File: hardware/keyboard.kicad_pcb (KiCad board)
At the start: 2 copper layers, 321.6 x 135 mm, 172 parts, among them J1 USB_OTG, U1 ATMEGA32U4-AU, U2 MCP23018_SSOP, Y1 16MHz

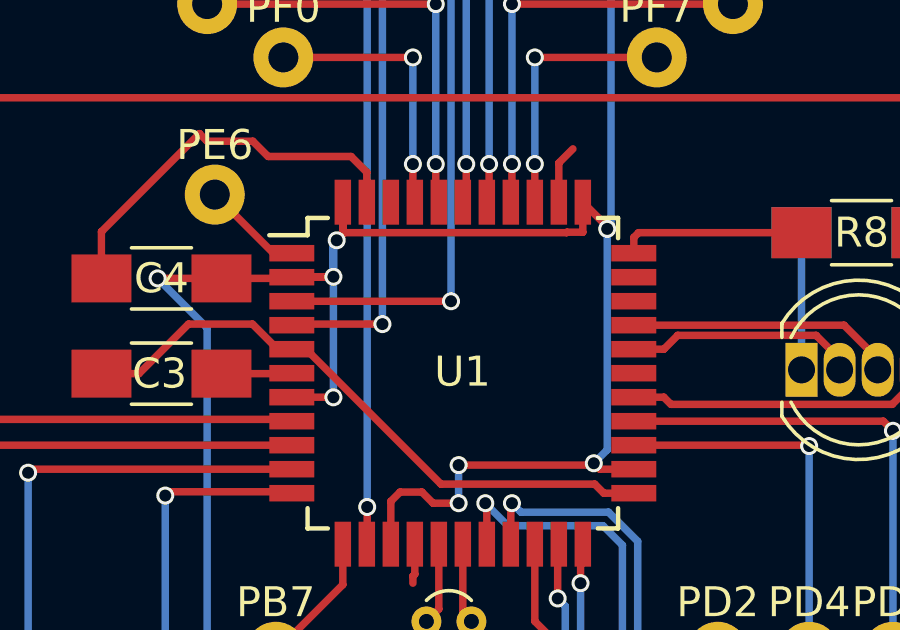
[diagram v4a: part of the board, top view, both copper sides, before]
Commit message: Update mounting hole references to ''
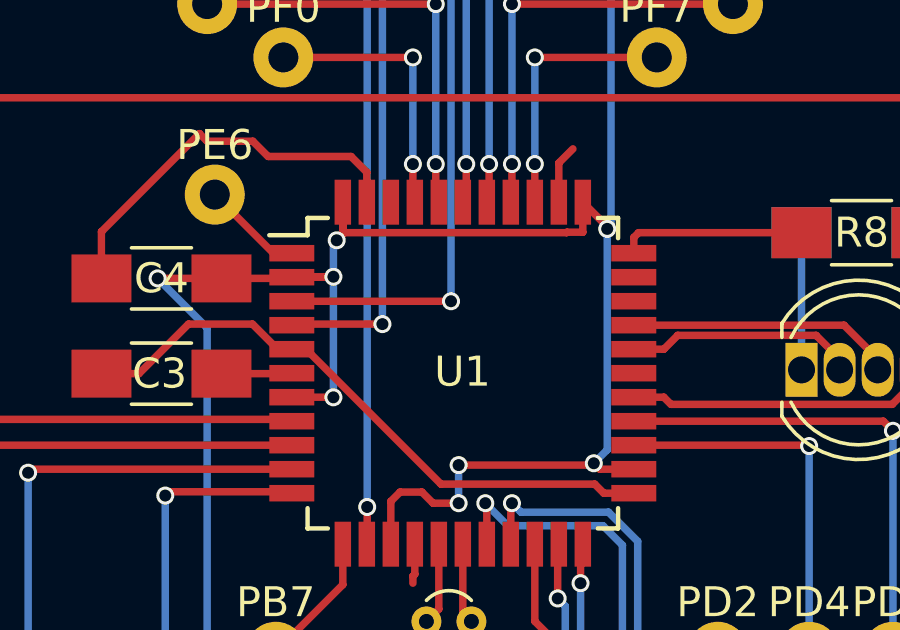
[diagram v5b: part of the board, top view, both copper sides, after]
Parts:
- removed REF** (x9): MountingHole_3.2mm_M3, MountingHole_3.2mm_M3
- added ?: MountingHole_3.2mm_M3, MountingHole_3.2mm_M3, F.Cu at (230.9, 148.9)
- added ?: MountingHole_3.2mm_M3, MountingHole_3.2mm_M3, F.Cu at (127.1, 148.9)
- added ?: MountingHole_3.2mm_M3, MountingHole_3.2mm_M3, F.Cu at (179.0, 155.9)
- added ?: MountingHole_3.2mm_M3, MountingHole_3.2mm_M3, F.Cu at (335.5, 130.5)
- added ?: MountingHole_3.2mm_M3, MountingHole_3.2mm_M3, F.Cu at (22.5, 130.5)
- added ?: MountingHole_3.2mm_M3, MountingHole_3.2mm_M3, F.Cu at (316.7, 28.9)
- added ?: MountingHole_3.2mm_M3, MountingHole_3.2mm_M3, F.Cu at (230.7, 28.9)
- added ?: MountingHole_3.2mm_M3, MountingHole_3.2mm_M3, F.Cu at (127.3, 28.9)
- added ?: MountingHole_3.2mm_M3, MountingHole_3.2mm_M3, F.Cu at (41.3, 28.9)
- renumbered D1 to ?
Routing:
- net +5V: track 141.4 -> 139.3 mm
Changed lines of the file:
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@@
     (links 256)
     (no_connects 0)
-    (area 13.09439 23.434285 344.905608 190.075001)
+    (area 0.254 20.32 347.218001 190.075001)
     (thickness 1.6)
-    (drawings 8)
-    (tracks 804)
+    (drawings 6)
+    (tracks 802)
     (zones 0)
     (modules 172)
@@
     (descr "Mounting Hole 3.2mm, no annular, M3")
     (tags "mounting hole 3.2mm no annular m3")
-    (fp_text reference REF** (at 0 -4.2) (layer F.SilkS) hide
+    (fp_text reference "" (at 0 -4.2) (layer F.SilkS)
       (effects (font (size 1 1) (thickness 0.15)))
     )
@@
     (descr "Mounting Hole 3.2mm, no annular, M3")
     (tags "mounting hole 3.2mm no annular m3")
-    (fp_text reference REF** (at 0 -4.2) (layer F.SilkS) hide
+    (fp_text reference "" (at 0 -4.2) (layer F.SilkS)
       (effects (font (size 1 1) (thickness 0.15)))
     )
@@
     (descr "Mounting Hole 3.2mm, no annular, M3")
     (tags "mounting hole 3.2mm no annular m3")
-    (fp_text reference REF** (at 0 -4.2) (layer F.SilkS) hide
+    (fp_text reference "" (at 0 -4.2) (layer F.SilkS)
       (effects (font (size 1 1) (thickness 0.15)))
     )
@@
     (descr "Mounting Hole 3.2mm, no annular, M3")
     (tags "mounting hole 3.2mm no annular m3")
-    (fp_text reference REF** (at 0 -4.2) (layer F.SilkS) hide
+    (fp_text reference "" (at 0 -4.2) (layer F.SilkS)
       (effects (font (size 1 1) (thickness 0.15)))
     )
@@
     (descr "Mounting Hole 3.2mm, no annular, M3")
     (tags "mounting hole 3.2mm no annular m3")
-    (fp_text reference REF** (at 0 -4.2) (layer F.SilkS) hide
+    (fp_text reference "" (at 0 -4.2) (layer F.SilkS)
       (effects (font (size 1 1) (thickness 0.15)))
     )
@@
     (descr "Mounting Hole 3.2mm, no annular, M3")
     (tags "mounting hole 3.2mm no annular m3")
-    (fp_text reference REF** (at 0 -4.2) (layer F.SilkS) hide
+    (fp_text reference "" (at 0 -4.2) (layer F.SilkS)
       (effects (font (size 1 1) (thickness 0.15)))
     )
@@
     (descr "Mounting Hole 3.2mm, no annular, M3")
     (tags "mounting hole 3.2mm no annular m3")
-    (fp_text reference REF** (at 0 -4.2) (layer F.SilkS) hide
+    (fp_text reference "" (at 0 -4.2) (layer F.SilkS)
       (effects (font (size 1 1) (thickness 0.15)))
     )
@@
     (descr "Mounting Hole 3.2mm, no annular, M3")
     (tags "mounting hole 3.2mm no annular m3")
-    (fp_text reference REF** (at 0 -4.2) (layer F.SilkS) hide
+    (fp_text reference "" (at 0 -4.2) (layer F.SilkS)
       (effects (font (size 1 1) (thickness 0.15)))
     )
@@
     (descr "Mounting Hole 3.2mm, no annular, M3")
     (tags "mounting hole 3.2mm no annular m3")
-    (fp_text reference REF** (at 0 -4.2) (layer F.SilkS) hide
+    (fp_text reference "" (at 0 -4.2) (layer F.SilkS)
       (effects (font (size 1 1) (thickness 0.15)))
     )
@@
     (tags SOD-123)
     (attr smd)
-    (fp_text reference D1 (at 0 2 170) (layer B.SilkS)
+    (fp_text reference "" (at 0 2 170) (layer B.SilkS)
       (effects (font (size 1 1) (thickness 0.15)) (justify mirror))
     )
@@
   (gr_line (start 18.191942 133.462701) (end 168.276643 159.926683) (layer Edge.Cuts) (width 0.15))
   (gr_line (start 37.336653 24.887647) (end 18.191942 133.462701) (layer Edge.Cuts) (width 0.15))
-  (gr_line (start 179 40) (end 179 190) (layer Dwgs.User) (width 0.15))
-  (gr_line (start 179 40) (end 179 190) (layer Dwgs.User) (width 0.15))
   (segment (start 182.664 73.368) (end 183.134 72.898) (width 0.25) (layer F.Cu) (net 1))
-  (segment (start 182.664 74.676) (end 182.664 73.368) (width 0.25) (layer F.Cu) (net 1))
+  (segment (start 182.664 74.676) (end 182.664 73.368) (width 0.25) (layer F.Cu) (net 1) (status 10))
   (segment (start 194.754 73.342) (end 194.564 73.152) (width 0.25) (layer F.Cu) (net 1))
-  (segment (start 194.754 75.692) (end 194.754 73.342) (width 0.25) (layer F.Cu) (net 1))
+  (segment (start 194.754 75.692) (end 194.754 73.342) (width 0.25) (layer F.Cu) (net 1) (status 10))
   (segment (start 178.737 84.074) (end 183.862 84.074) (width 0.25) (layer F.Cu) (net 1))
   (segment (start 183.862 84.074) (end 184.164 84.376) (width 0.25) (layer F.Cu) (net 1))
-  (segment (start 184.164 84.376) (end 185.164 84.376) (width 0.25) (layer F.Cu) (net 1))
-  (segment (start 173.764 79.576) (end 174.239 79.576) (width 0.25) (layer F.Cu) (net 1))
-  (segment (start 174.239 79.576) (end 178.737 84.074) (width 0.25) (layer F.Cu) (net 1))
+  (segment (start 184.164 84.376) (end 185.164 84.376) (width 0.25) (layer F.Cu) (net 1) (status 20))
+  (segment (start 173.764 79.576) (end 174.239 79.576) (width 0.25) (layer F.Cu) (net 1) (status 30))
+  (segment (start 174.239 79.576) (end 178.737 84.074) (width 0.25) (layer F.Cu) (net 1) (status 10))
   (segment (start 177.8 87.14) (end 177.8 87.376) (width 0.25) (layer F.Cu) (net 1))
-  (segment (start 177.864 86.076) (end 177.864 87.076) (width 0.25) (layer F.Cu) (net 1))
+  (segment (start 177.864 86.076) (end 177.864 87.076) (width 0.25) (layer F.Cu) (net 1) (status 10))
   (segment (start 177.864 87.076) (end 177.8 87.14) (width 0.25) (layer F.Cu) (net 1))
   (segment (start 176.948 110.58) (end 181.07 106.458) (width 0.25) (layer F.Cu) (net 1))
-  (segment (start 181.07 106.458) (end 181.07 102.362) (width 0.25) (layer F.Cu) (net 1))
-  (segment (start 175.21 110.58) (end 176.948 110.58) (width 0.25) (layer F.Cu) (net 1))
+  (segment (start 181.07 106.458) (end 181.07 102.362) (width 0.25) (layer F.Cu) (net 1) (status 20))
+  (segment (start 175.21 110.58) (end 176.948 110.58) (width 0.25) (layer F.Cu) (net 1) (status 10))
   (segment (start 170.686 72.39) (end 167.418 75.658) (width 0.25) (layer F.Cu) (net 1))
-  (segment (start 167.418 75.658) (end 167.418 77.216) (width 0.25) (layer F.Cu) (net 1))
+  (segment (start 167.418 75.658) (end 167.418 77.216) (width 0.25) (layer F.Cu) (net 1) (status 20))
   (segment (start 172.466 72.644) (end 170.94 72.644) (width 0.25) (layer F.Cu) (net 1))
   (segment (start 170.94 72.644) (end 170.686 72.39) (width 0.25) (layer F.Cu) (net 1))
   (segment (start 172.974 73.152) (end 172.466 72.644) (width 0.25) (layer F.Cu) (net 1))
   (segment (start 175.74 73.152) (end 172.974 73.152) (width 0.25) (layer F.Cu) (net 1))
-  (segment (start 176.264 74.676) (end 176.264 73.676) (width 0.25) (layer F.Cu) (net 1))
+  (segment (start 176.264 74.676) (end 176.264 73.676) (width 0.25) (layer F.Cu) (net 1) (status 10))
   (segment (start 176.264 73.676) (end 175.74 73.152) (width 0.25) (layer F.Cu) (net 1))
   (segment (start 172.453 78.74) (end 170.319 78.74) (width 0.25) (layer F.Cu) (net 1))
   (segment (start 170.319 78.74) (end 168.668 80.391) (width 0.25) (layer F.Cu) (net 1))
-  (segment (start 168.668 80.391) (end 167.418 80.391) (width 0.25) (layer F.Cu) (net 1))
-  (segment (start 173.764 79.576) (end 173.289 79.576) (width 0.25) (layer F.Cu) (net 1))
-  (segment (start 173.289 79.576) (end 172.453 78.74) (width 0.25) (layer F.Cu) (net 1))
+  (segment (start 168.668 80.391) (end 167.418 80.391) (width 0.25) (layer F.Cu) (net 1) (status 20))
+  (segment (start 173.764 79.576) (end 173.289 79.576) (width 0.25) (layer F.Cu) (net 1) (status 30))
+  (segment (start 173.289 79.576) (end 172.453 78.74) (width 0.25) (layer F.Cu) (net 1) (status 10))
   (segment (start 181.5 91) (end 181.5 90.8) (width 0.25) (layer F.Cu) (net 2) (status 30))
   (segment (start 181.5 90.8) (end 179.75 89.05) (width 0.25) (layer F.Cu) (net 2) (status 30))
@@
   (segment (start 178.664 86.076) (end 178.664 88.236) (width 0.25) (layer F.Cu) (net 3) (status 10))
   (segment (start 178.664 88.236) (end 178.25 88.65) (width 0.25) (layer F.Cu) (net 3) (status 20))
-  (segment (start 175.464 74.676) (end 175.464 75.742) (width 0.25) (layer F.Cu) (net 4))
+  (segment (start 175.464 74.676) (end 175.464 75.742) (width 0.25) (layer F.Cu) (net 4) (status 10))
   (segment (start 175.464 75.742) (end 175.26 75.946) (width 0.25) (layer F.Cu) (net 4))
   (segment (start 175.15 77.16) (end 175.15 76.056) (width 0.25) (layer B.Cu) (net 4))
   (segment (start 175.15 76.056) (end 175.26 75.946) (width 0.25) (layer B.Cu) (net 4))
-  (segment (start 175.15 77.16) (end 175.15 76.09) (width 0.25) (layer B.Cu) (net 4))
-  (segment (start 175.15 81.18) (end 175.15 76.09) (width 0.25) (layer B.Cu) (net 4))
-  (segment (start 173.764 77.176) (end 175.134 77.176) (width 0.25) (layer F.Cu) (net 4))
+  (segment (start 175.15 77.16) (end 175.15 81.18) (width 0.25) (layer B.Cu) (net 4))
+  (segment (start 173.764 77.176) (end 175.134 77.176) (width 0.25) (layer F.Cu) (net 4) (status 10))
   (segment (start 175.134 77.176) (end 175.15 77.16) (width 0.25) (layer F.Cu) (net 4))
   (segment (start 184.404 38.862) (end 184.404 75.438) (width 0.25) (layer B.Cu) (net 4) (status 10))
@@
   (segment (start 181.61 38.862) (end 184.404 38.862) (width 0.25) (layer F.Cu) (net 4) (status 30))
   (via (at 175.15 77.16) (size 0.6) (drill 0.4) (layers F.Cu B.Cu) (net 4))
-  (segment (start 175.514 75.692) (end 182.923 75.692) (width 0.25) (layer F.Cu) (net 4))
+  (segment (start 175.48 75.692) (end 182.923 75.692) (width 0.25) (layer F.Cu) (net 4))
   (segment (start 175.464 74.676) (end 175.464 75.676) (width 0.25) (layer F.Cu) (net 4) (status 10))
   (segment (start 175.464 75.676) (end 175.48 75.692) (width 0.25) (layer F.Cu) (net 4))
-  (segment (start 175.48 75.692) (end 175.514 75.692) (width 0.25) (layer F.Cu) (net 4))
   (segment (start 182.923 75.692) (end 182.939 75.676) (width 0.25) (layer F.Cu) (net 4))
   (segment (start 182.939 75.676) (end 183.464 75.676) (width 0.25) (layer F.Cu) (net 4))

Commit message: finish V2
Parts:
- removed the ? at (41.8, 36.9)
- removed D65: LED_CRGB, LEDs:LED_D5.0mm-4
- removed GND, SCL, SDA, VCC: CONN_01X01, keyboard-modules:CONN_1
- added D1: D_Small, Diodes_SMD:D_SOD-123, B.Cu at (41.8, 36.9)
- added D99: LED_ARGB, LEDs:LED_D5.0mm-4-v2, F.Cu at (166.9, 35.8)
- added R1: 1k, Resistors_SMD:R_1206_HandSoldering, F.Cu at (166.6, 42.4)
- added R3: 1k, Resistors_SMD:R_1206_HandSoldering, F.Cu at (171.2, 42.4)
- R2: moved to F.Cu
- moved R2 41.0 mm to (168.9, 42.4), turned to 270 degrees
- moved R8 5.15 mm to (187.7, 74.7), turned to 270 degrees
- moved D61 0.25 mm to (149.6, 134.1)
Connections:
- R2 pad 2: GND -> LED2
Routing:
- net LED3: track 10.2 -> 70.4 mm, vias 0 -> 2
- net LED2: track 9.32 -> 65.7 mm, vias 0 -> 2
- net LED1: track 7.85 -> 63.7 mm, vias 0 -> 2
- net +5V: track 139.3 -> 155.9 mm, vias 11 -> 12
- net GND: track 51.6 -> 62.7 mm
- net Net-(D99-Pad2): track 0.00 -> 5.04 mm
- net Net-(D99-Pad4): track 0.00 -> 4.78 mm
- net Net-(R8-Pad2): track 6.29 -> 2.78 mm
- net SDA: track 43.7 -> 42.3 mm
- net SCL: track 42.5 -> 41.1 mm
- net Net-(D62-Pad2): track 3.30 -> 4.18 mm

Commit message: Update schematic, WIP fixes + adding test points
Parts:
- removed ? (x9): MountingHole_3.2mm_M3, MountingHole_3.2mm_M3
- removed PB7, PD2, PD3, PD4, PD5, PD6, PE6, PF0, PF1, PF4, PF5, PF6, PF7: CONN_01X01, keyboard-modules:CONN_1
- added J2: CONN_01X05, Pin_Headers:Pin_Header_Straight_1x05_Pitch1.27mm, F.Cu at (156.5, 81.5)
- added J3: CONN_01X04, Pin_Headers:Pin_Header_Straight_1x04_Pitch1.27mm, F.Cu at (187.7, 99.3)
- added J4: CONN_01X07, Pin_Headers:Pin_Header_Straight_1x07_Pitch1.27mm, F.Cu at (159.5, 60.2)
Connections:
- net Net-(R8-Pad2) renamed /PE2
- U1 pad 1: /PE6 -> (no net)
- U1 pad 12: Net-(PB7-Pad1) -> ROW4
- U1 pad 20: /PD2 -> (no net)
- U1 pad 21: /PD3 -> (no net)
- U1 pad 22: /PD5 -> (no net)
- U1 pad 25: /PD4 -> (no net)
- U1 pad 26: /PD6 -> (no net)
- U1 pad 27: LED3 -> (no net)
- U1 pad 28: (no net) -> LED1
- U1 pad 29: LED1 -> LED2
- U1 pad 30: LED2 -> LED3
- U1 pad 40: /PF1 -> (no net)
- U1 pad 41: /PF0 -> (no net)
- U2 pad 1: +5V -> GND
- U2 pad 10: GND -> +5V
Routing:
- net ROW4: track 0.00 -> 19.2 mm, vias 0 -> 1
- net /PD6: track 16.1 -> 0.00 mm, vias 1 -> 0
- net /PD5: track 14.5 -> 0.00 mm, vias 2 -> 0
- net /PF4: track 14.5 -> 0.16 mm, vias 2 -> 0
- net /PF1: track 14.3 -> 0.00 mm, vias 2 -> 0
- net /PF6: track 14.0 -> 0.05 mm, vias 2 -> 0
- net /PF5: track 14.0 -> 0.11 mm, vias 2 -> 0
- net ROW3: track 396.4 -> 409.8 mm
- net /PD4: track 12.7 -> 0.00 mm, vias 1 -> 0
- net /PD3: track 12.6 -> 0.00 mm, vias 2 -> 0
- net /PF0: track 9.17 -> 0.00 mm, vias 2 -> 0
- net /PD2: track 9.09 -> 0.00 mm
- net /PF7: track 8.89 -> 0.00 mm, vias 2 -> 0
- net ROW2: track 359.4 -> 368.0 mm
- net LED3: track 70.4 -> 78.0 mm
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- removed copper zone on B.Cu, net GND
- removed copper zone on F.Cu, net GND

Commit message: Add mounting holes back
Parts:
- added ?: MountingHole_3.2mm_M3, MountingHole_3.2mm_M3, F.Cu at (230.9, 148.9)
- added ?: MountingHole_3.2mm_M3, MountingHole_3.2mm_M3, F.Cu at (127.1, 148.9)
- added ?: MountingHole_3.2mm_M3, MountingHole_3.2mm_M3, F.Cu at (179.0, 155.9)
- added ?: MountingHole_3.2mm_M3, MountingHole_3.2mm_M3, F.Cu at (335.5, 130.5)
- added ?: MountingHole_3.2mm_M3, MountingHole_3.2mm_M3, F.Cu at (22.5, 130.5)
- added ?: MountingHole_3.2mm_M3, MountingHole_3.2mm_M3, F.Cu at (316.7, 28.9)
- added ?: MountingHole_3.2mm_M3, MountingHole_3.2mm_M3, F.Cu at (230.7, 28.9)
- added ?: MountingHole_3.2mm_M3, MountingHole_3.2mm_M3, F.Cu at (127.3, 28.9)
- added ?: MountingHole_3.2mm_M3, MountingHole_3.2mm_M3, F.Cu at (41.3, 28.9)
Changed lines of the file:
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@@
   (general
     (links 256)
-    (no_connects 21)
-    (area 18.116941 24.812646 339.883057 160.001684)
+    (no_connects 20)
+    (area 13.09439 23.434285 344.905608 161.001683)
     (thickness 1.6)
     (drawings 6)
     (tracks 785)
     (zones 0)
-    (modules 151)
+    (modules 160)
     (nets 109)
   )
@@
     (add_net SDA)
   )
+  (module MountingHole_3.2mm_M3 (layer F.Cu)
+    (at 230.863401 148.938904)
+    (descr "Mounting Hole 3.2mm, no annular, M3")
+    (tags "mounting hole 3.2mm no annular m3")
+    (fp_text reference "" (at 0 -4.2) (layer F.SilkS)
+      (effects (font (size 1 1) (thickness 0.15)))
+    )
+    (fp_text value MountingHole_3.2mm_M3 (at 0 4.2) (layer F.Fab)
+      (effects (font (size 1 1) (thickness 0.15)))
+    )
+    (fp_circle (center 0 0) (end 3.45 0) (layer F.CrtYd) (width 0.05))
+    (fp_circle (center 0 0) (end 3.2 0) (layer Cmts.User) (width 0.15))
+    (pad 1 np_thru_hole circle (at 0 0) (size 3.2 3.2) (drill 3.2) (layers *.Cu *.Mask))
+  )
+  (module MountingHole_3.2mm_M3 (layer F.Cu)
+    (at 127.136596 148.938904)
+    (descr "Mounting Hole 3.2mm, no annular, M3")
+    (tags "mounting hole 3.2mm no annular m3")
+    (fp_text reference "" (at 0 -4.2) (layer F.SilkS)
+      (effects (font (size 1 1) (thickness 0.15)))
+    )
+    (fp_text value MountingHole_3.2mm_M3 (at 0 4.2) (layer F.Fab)
+      (effects (font (size 1 1) (thickness 0.15)))
+    )
+    (fp_circle (center 0 0) (end 3.45 0) (layer F.CrtYd) (width 0.05))
+    (fp_circle (center 0 0) (end 3.2 0) (layer Cmts.User) (width 0.15))
+    (pad 1 np_thru_hole circle (at 0 0) (size 3.2 3.2) (drill 3.2) (layers *.Cu *.Mask))
+  )
+  (module MountingHole_3.2mm_M3 (layer F.Cu)
+    (at 178.999998 155.926683)
+    (descr "Mounting Hole 3.2mm, no annular, M3")
+    (tags "mounting hole 3.2mm no annular m3")
+    (fp_text reference "" (at 0 -4.2) (layer F.SilkS)
+      (effects (font (size 1 1) (thickness 0.15)))
+    )
+    (fp_text value MountingHole_3.2mm_M3 (at 0 4.2) (layer F.Fab)
+      (effects (font (size 1 1) (thickness 0.15)))
+    )
+    (fp_circle (center 0 0) (end 3.45 0) (layer F.CrtYd) (width 0.05))
+    (fp_circle (center 0 0) (end 3.2 0) (layer Cmts.User) (width 0.15))
+    (pad 1 np_thru_hole circle (at 0 0) (size 3.2 3.2) (drill 3.2) (layers *.Cu *.Mask))
+  )
+  (module MountingHole_3.2mm_M3 (layer F.Cu)
+    (at 335.548465 130.480103)
+    (descr "Mounting Hole 3.2mm, no annular, M3")
+    (tags "mounting hole 3.2mm no annular m3")
+    (fp_text reference "" (at 0 -4.2) (layer F.SilkS)
+      (effects (font (size 1 1) (thickness 0.15)))
+    )
+    (fp_text value MountingHole_3.2mm_M3 (at 0 4.2) (layer F.Fab)
+      (effects (font (size 1 1) (thickness 0.15)))
+    )
+    (fp_circle (center 0 0) (end 3.45 0) (layer F.CrtYd) (width 0.05))
+    (fp_circle (center 0 0) (end 3.2 0) (layer Cmts.User) (width 0.15))
+    (pad 1 np_thru_hole circle (at 0 0) (size 3.2 3.2) (drill 3.2) (layers *.Cu *.Mask))
+  )
+  (module MountingHole_3.2mm_M3 (layer F.Cu)
+    (at 22.451533 130.480103)
+    (descr "Mounting Hole 3.2mm, no annular, M3")
+    (tags "mounting hole 3.2mm no annular m3")
+    (fp_text reference "" (at 0 -4.2) (layer F.SilkS)
+      (effects (font (size 1 1) (thickness 0.15)))
+    )
+    (fp_text value MountingHole_3.2mm_M3 (at 0 4.2) (layer F.Fab)
+      (effects (font (size 1 1) (thickness 0.15)))
+    )
+    (fp_circle (center 0 0) (end 3.45 0) (layer F.CrtYd) (width 0.05))
+    (fp_circle (center 0 0) (end 3.2 0) (layer Cmts.User) (width 0.15))
+    (pad 1 np_thru_hole circle (at 0 0) (size 3.2 3.2) (drill 3.2) (layers *.Cu *.Mask))
+  )
+  (module MountingHole_3.2mm_M3 (layer F.Cu)
+    (at 316.663345 28.887647)
+    (descr "Mounting Hole 3.2mm, no annular, M3")
+    (tags "mounting hole 3.2mm no annular m3")
+    (fp_text reference "" (at 0 -4.2) (layer F.SilkS)
+      (effects (font (size 1 1) (thickness 0.15)))
+    )
+    (fp_text value MountingHole_3.2mm_M3 (at 0 4.2) (layer F.Fab)
+      (effects (font (size 1 1) (thickness 0.15)))
+    )
+    (fp_circle (center 0 0) (end 3.45 0) (layer F.CrtYd) (width 0.05))
+    (fp_circle (center 0 0) (end 3.2 0) (layer Cmts.User) (width 0.15))
+    (pad 1 np_thru_hole circle (at 0 0) (size 3.2 3.2) (drill 3.2) (layers *.Cu *.Mask))
+  )
+  (module MountingHole_3.2mm_M3 (layer F.Cu)
+    (at 230.663345 28.887647)
+    (descr "Mounting Hole 3.2mm, no annular, M3")
+    (tags "mounting hole 3.2mm no annular m3")
+    (fp_text reference "" (at 0 -4.2) (layer F.SilkS)
+      (effects (font (size 1 1) (thickness 0.15)))
+    )
+    (fp_text value MountingHole_3.2mm_M3 (at 0 4.2) (layer F.Fab)
+      (effects (font (size 1 1) (thickness 0.15)))
+    )
+    (fp_circle (center 0 0) (end 3.45 0) (layer F.CrtYd) (width 0.05))
+    (fp_circle (center 0 0) (end 3.2 0) (layer Cmts.User) (width 0.15))
+    (pad 1 np_thru_hole circle (at 0 0) (size 3.2 3.2) (drill 3.2) (layers *.Cu *.Mask))
+  )
+  (module MountingHole_3.2mm_M3 (layer F.Cu)
+    (at 127.336653 28.887647)
+    (descr "Mounting Hole 3.2mm, no annular, M3")
+    (tags "mounting hole 3.2mm no annular m3")
+    (fp_text reference "" (at 0 -4.2) (layer F.SilkS)
+      (effects (font (size 1 1) (thickness 0.15)))
+    )
+    (fp_text value MountingHole_3.2mm_M3 (at 0 4.2) (layer F.Fab)
+      (effects (font (size 1 1) (thickness 0.15)))
+    )
+    (fp_circle (center 0 0) (end 3.45 0) (layer F.CrtYd) (width 0.05))
+    (fp_circle (center 0 0) (end 3.2 0) (layer Cmts.User) (width 0.15))
+    (pad 1 np_thru_hole circle (at 0 0) (size 3.2 3.2) (drill 3.2) (layers *.Cu *.Mask))
+  )
+  (module MountingHole_3.2mm_M3 (layer F.Cu)
+    (at 41.336653 28.887647)
+    (descr "Mounting Hole 3.2mm, no annular, M3")
+    (tags "mounting hole 3.2mm no annular m3")
+    (fp_text reference "" (at 0 -4.2) (layer F.SilkS)
+      (effects (font (size 1 1) (thickness 0.15)))
+    )
+    (fp_text value MountingHole_3.2mm_M3 (at 0 4.2) (layer F.Fab)
+      (effects (font (size 1 1) (thickness 0.15)))
+    )
+    (fp_circle (center 0 0) (end 3.45 0) (layer F.CrtYd) (width 0.05))
+    (fp_circle (center 0 0) (end 3.2 0) (layer Cmts.User) (width 0.15))
+    (pad 1 np_thru_hole circle (at 0 0) (size 3.2 3.2) (drill 3.2) (layers *.Cu *.Mask))
+  )
   (module Crystals:Crystal_Round_d1.0mm_Vertical (layer F.Cu)
